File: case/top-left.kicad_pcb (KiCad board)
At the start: 2 copper layers, 135 x 95.7 mm, 28 parts, among them SW1 SW_PUSH, SW10 SW_PUSH, SW11 SW_PUSH, SW12 SW_PUSH, SW13 SW_PUSH, SW14 SW_PUSH, SW15 SW_PUSH, SW16 SW_PUSH, SW17 SW_PUSH, SW18 SW_PUSH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

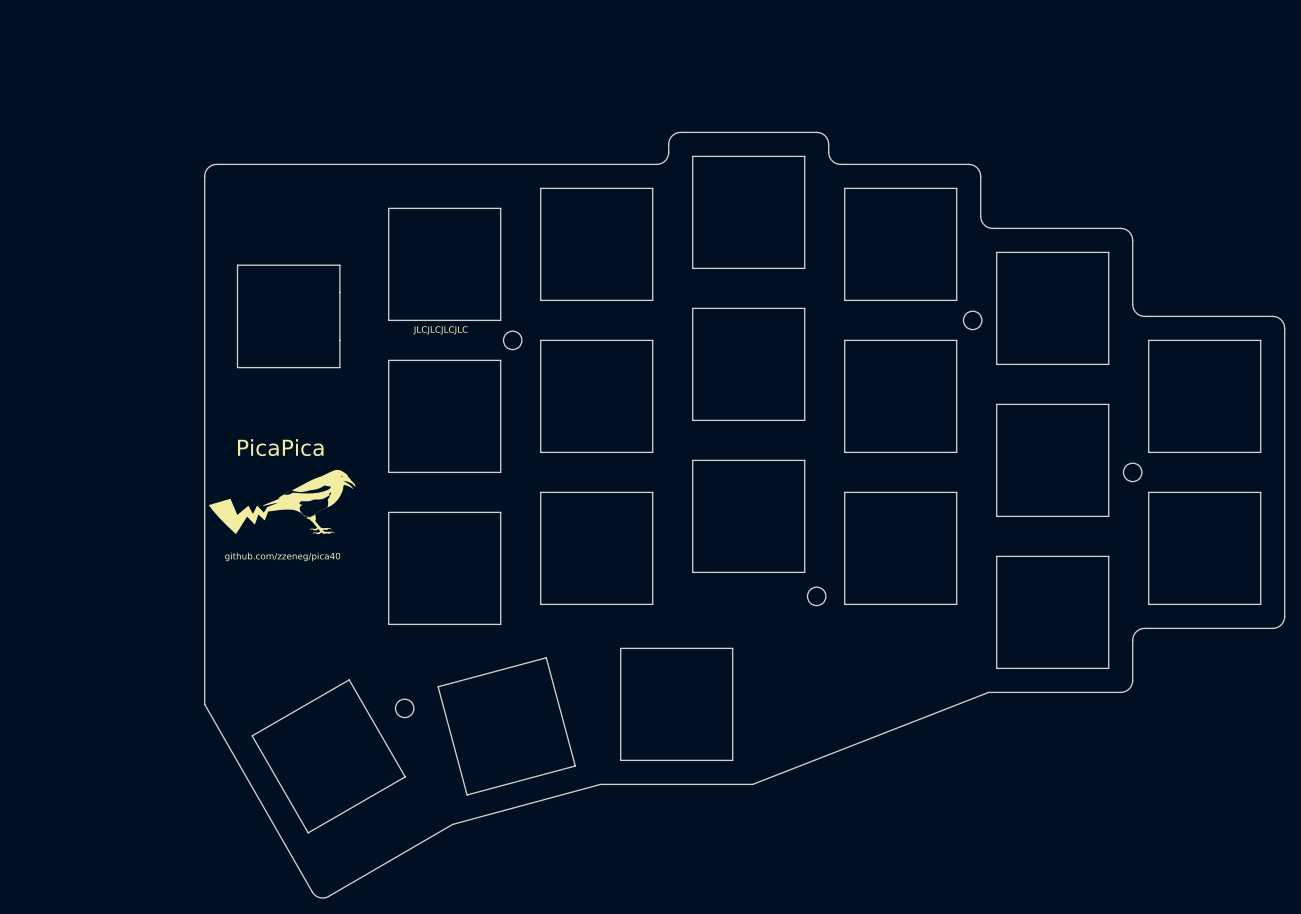
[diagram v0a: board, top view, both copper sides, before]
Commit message: update cases, extra hole on right side
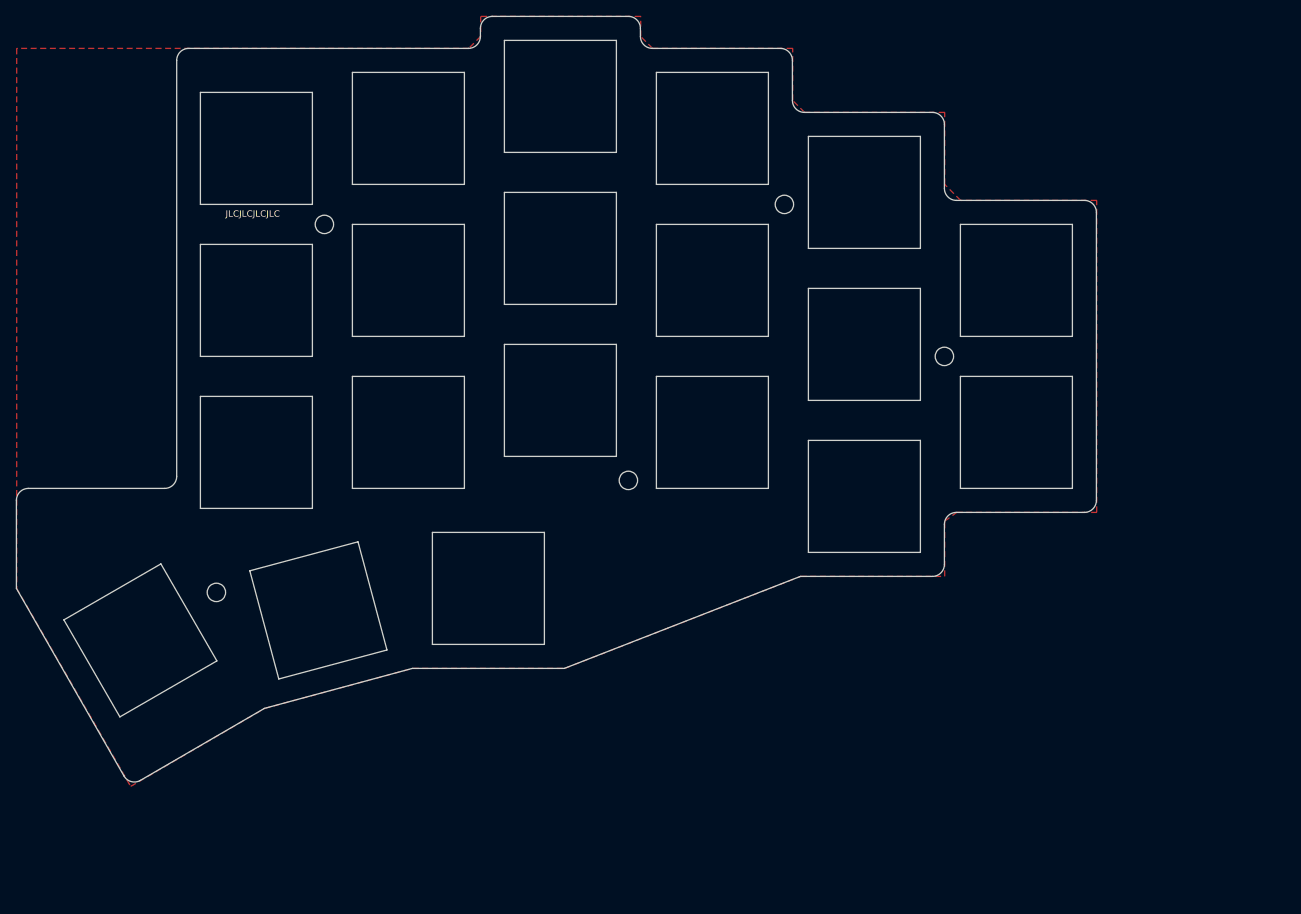
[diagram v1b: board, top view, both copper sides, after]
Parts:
- removed G***: LOGO, pica:logo_mirror
- removed G***: LOGO, pica:logo
- removed RE1: RotaryEncoder_Switch, pica:EC11_Hole
- moved H1 27.6 mm to (140.5, 62.0)
- moved H2 27.6 mm to (69.5, 110.5)
- moved H3 27.6 mm to (160.5, 81.0)
- moved H4 27.6 mm to (121.0, 96.5)
- moved H5 27.6 mm to (83.0, 64.5)
- moved SW1 27.6 mm to (150.5, 60.5)
- moved SW10 27.6 mm to (74.5, 74.0)
- moved SW11 27.6 mm to (150.5, 98.5)
- moved SW12 27.6 mm to (131.5, 90.5)
- moved SW13 27.6 mm to (112.5, 86.5)
- moved SW14 27.6 mm to (93.5, 90.5)
- moved SW15 27.6 mm to (74.5, 93.0)
- moved SW16 27.6 mm to (169.5, 71.5)
- moved SW17 27.6 mm to (169.5, 90.5)
- moved SW18 27.6 mm to (103.5, 110.0)
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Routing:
- added copper zone on F.Cu, net (none)
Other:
- outline, holes or cut-outs redrawn
- board text removed: "PicaPica"
- board text removed: "github.com/zzeneg/pica40"
